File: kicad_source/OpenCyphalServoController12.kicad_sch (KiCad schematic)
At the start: 46 parts, among them CN1 RASPBERRYPI_PICO, CN2 SM04B-SRSS-TB, CN3 SM04B-SRSS-TB, CN7 CONN_02X03, SW1 SPST, U3 24LC64

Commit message: started first placement
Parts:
- gave numbers to parts that had none: 21
- renumbered C6 to C1, C9 to C3, CN2 to CN1, CN7 to CN2, CN3 to CN8, CN1 to CN9, D5 to D1, D4 to D2, R11 to R1, R13 to R17, R14 to R18, R16 to R19, R15 to R22, R9 to R7, R10 to R8, R12 to R9, U3 to U1

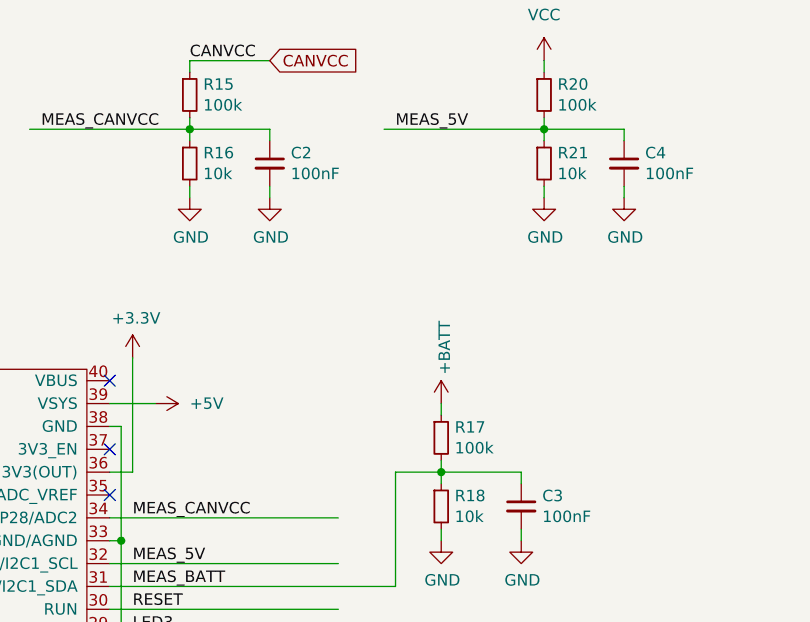
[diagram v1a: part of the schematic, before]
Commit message: corrected resistor dividers for voltage measurement
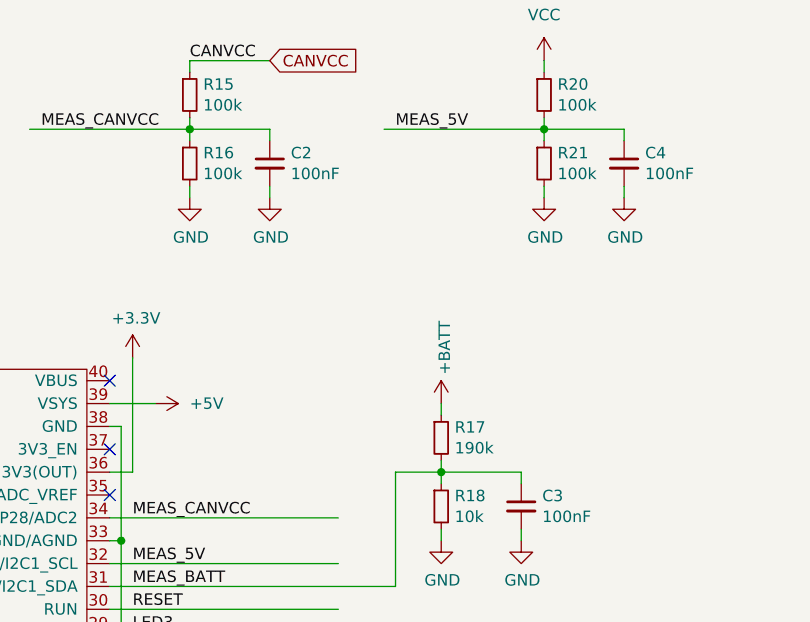
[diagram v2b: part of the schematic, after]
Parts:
- R16, R21: value 10k -> 100k
- R17: value 100k -> 190k
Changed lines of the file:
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@@
   (title_block
     (title "OpenCyphalServoController12")
-    (date "2023-01-23")
+    (date "2023-02-03")
     (rev "0.1")
     (company "generationmake")
@@
       (effects (font (size 1.27 1.27)) (justify left))
     )
-    (property "Value" "100k" (id 1) (at 245.3386 72.263 0)
+    (property "Value" "190k" (id 1) (at 245.3386 72.263 0)
       (effects (font (size 1.27 1.27)) (justify left))
     )
@@
       (effects (font (size 1.27 1.27)) (justify left))
     )
-    (property "Value" "10k" (id 1) (at 217.3986 41.783 0)
+    (property "Value" "100k" (id 1) (at 217.3986 41.783 0)
       (effects (font (size 1.27 1.27)) (justify left))
     )
@@
       (effects (font (size 1.27 1.27)) (justify left))
     )
-    (property "Value" "10k" (id 1) (at 256.7686 41.783 0)
+    (property "Value" "100k" (id 1) (at 256.7686 41.783 0)
       (effects (font (size 1.27 1.27)) (justify left))
     )
@@
     )
     (path "/98af084b-1d38-47e5-ba4f-133aa91a9cd0"
-      (reference "R16") (unit 1) (value "10k") (footprint "Resistor_SMD:R_0603_1608Metric")
+      (reference "R16") (unit 1) (value "100k") (footprint "Resistor_SMD:R_0603_1608Metric")
     )
     (path "/00000000-0000-0000-0000-000062580a99"
-      (reference "R17") (unit 1) (value "100k") (footprint "Resistor_SMD:R_0603_1608Metric")
+      (reference "R17") (unit 1) (value "190k") (footprint "Resistor_SMD:R_0603_1608Metric")
     )
     (path "/00000000-0000-0000-0000-000062580f1d"
@@
     )
     (path "/ff297292-bcb8-44b1-8fc4-6cf1ba8617ce"
-      (reference "R21") (unit 1) (value "10k") (footprint "Resistor_SMD:R_0603_1608Metric")
+      (reference "R21") (unit 1) (value "100k") (footprint "Resistor_SMD:R_0603_1608Metric")
     )
     (path "/00000000-0000-0000-0000-0000625730ad"

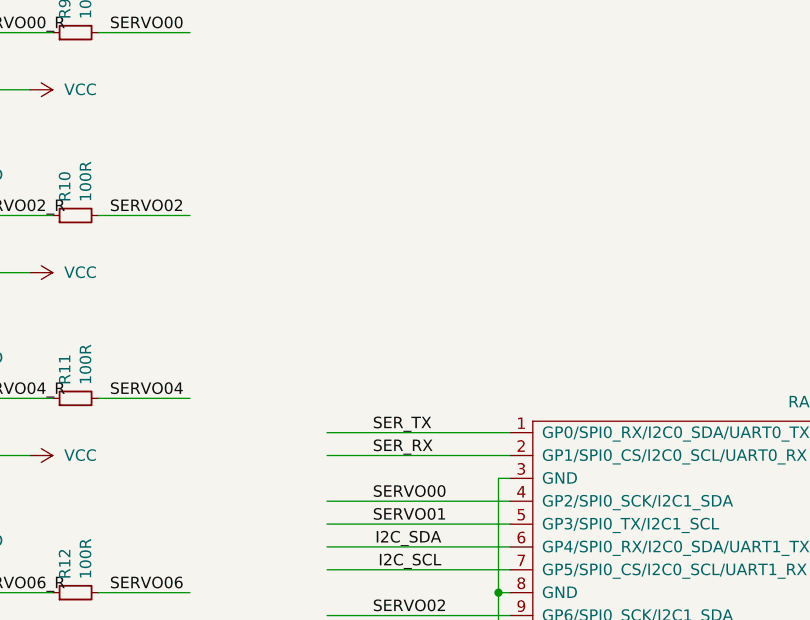
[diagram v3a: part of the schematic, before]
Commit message: added enable and power good for voltage regulator
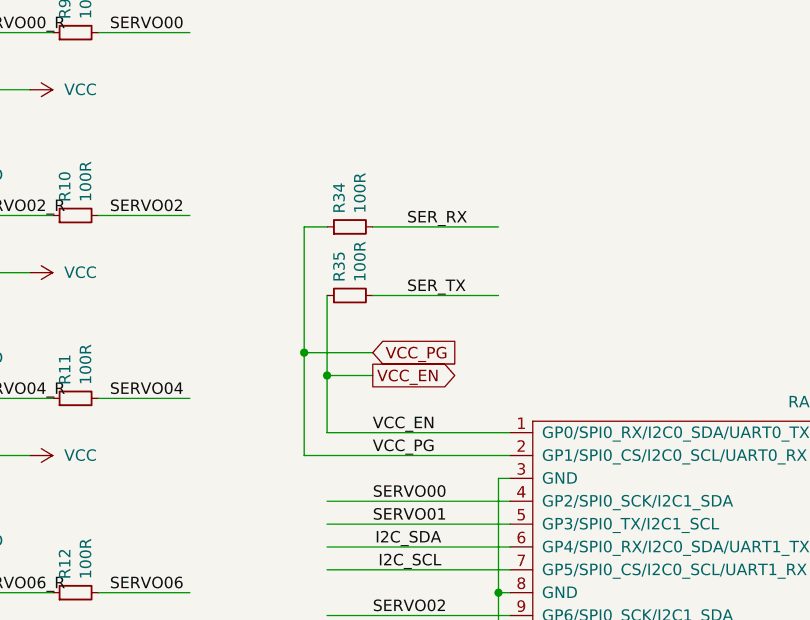
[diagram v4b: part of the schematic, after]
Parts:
- added R34, R35: 100R, Resistor_SMD:R_0603_1608Metric, symbol Device:R_Small
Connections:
- net SER_RX: now also R34.2; no longer CN9.2 (GP1/SPI0_CS/I2C0_SCL/UART0_RX)
- net SER_TX: now also R35.2; no longer CN9.1 (GP0/SPI0_RX/I2C0_SDA/UART0_TX)
- new net VCC_EN: CN9.1 (GP0/SPI0_RX/I2C0_SDA/UART0_TX), R35.1
- new net VCC_PG: CN9.2 (GP1/SPI0_CS/I2C0_SCL/UART0_RX), R34.1
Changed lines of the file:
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@@
   (junction (at 215.9 36.83) (diameter 0) (color 0 0 0 0)
   )
+  (junction (at 107.95 58.42) (diameter 0) (color 0 0 0 0)
+  )
   (junction (at 95.25 181.61) (diameter 0) (color 0 0 0 0)
   )
@@
   )
   (junction (at 208.28 82.55) (diameter 0) (color 0 0 0 0)
+  )
+  (junction (at 105.41 55.88) (diameter 0) (color 0 0 0 0)
   )
   (junction (at 95.25 179.07) (diameter 0) (color 0 0 0 0)
@@
     (stroke (width 0) (type default) (color 0 0 0 0))
   )
+  (wire (pts (xy 105.41 67.31) (xy 105.41 55.88))
+    (stroke (width 0) (type default) (color 0 0 0 0))
+  )
   (wire (pts (xy 215.9 38.1) (xy 215.9 36.83))
     (stroke (width 0) (type default) (color 0 0 0 0))
@@
     (stroke (width 0) (type default) (color 0 0 0 0))
   )
-  (wire (pts (xy 107.95 67.31) (xy 128.27 67.31))
-    (stroke (width 0) (type default) (color 0 0 0 0))
-  )
   (wire (pts (xy 95.25 176.53) (xy 95.25 179.07))
     (stroke (width 0) (type default) (color 0 0 0 0))
@@
     (stroke (width 0) (type default) (color 0 0 0 0))
   )
+  (wire (pts (xy 107.95 58.42) (xy 113.03 58.42))
+    (stroke (width 0) (type default) (color 0 0 0 0))
+  )
   (wire (pts (xy 27.94 123.19) (xy 38.1 123.19))
     (stroke (width 0) (type default) (color 0 0 0 0))
@@
     (stroke (width 0) (type default) (color 0 0 0 0))
   )
+  (wire (pts (xy 113.03 41.91) (xy 127 41.91))
+    (stroke (width 0) (type default) (color 0 0 0 0))
+  )
+  (wire (pts (xy 105.41 41.91) (xy 107.95 41.91))
+    (stroke (width 0) (type default) (color 0 0 0 0))
+  )
   (wire (pts (xy 53.34 106.68) (xy 54.61 106.68))
     (stroke (width 0) (type default) (color 0 0 0 0))
@@
     (stroke (width 0) (type default) (color 0 0 0 0))
   )
+  (wire (pts (xy 105.41 55.88) (xy 105.41 41.91))
+    (stroke (width 0) (type default) (color 0 0 0 0))
+  )
   (wire (pts (xy 228.6 105.41) (xy 207.01 105.41))
     (stroke (width 0) (type default) (color 0 0 0 0))
@@
     (stroke (width 0) (type default) (color 0 0 0 0))
   )
+  (wire (pts (xy 113.03 49.53) (xy 127 49.53))
+    (stroke (width 0) (type default) (color 0 0 0 0))
+  )
   (wire (pts (xy 237.49 36.83) (xy 255.27 36.83))
     (stroke (width 0) (type default) (color 0 0 0 0))
@@
     (stroke (width 0) (type default) (color 0 0 0 0))
   )
+  (wire (pts (xy 105.41 67.31) (xy 128.27 67.31))
+    (stroke (width 0) (type default) (color 0 0 0 0))
+  )
   (wire (pts (xy 68.58 40.64) (xy 68.58 44.45))
     (stroke (width 0) (type default) (color 0 0 0 0))
@@
     (stroke (width 0) (type default) (color 0 0 0 0))
   )
+  (wire (pts (xy 107.95 49.53) (xy 107.95 58.42))
+    (stroke (width 0) (type default) (color 0 0 0 0))
+  )
   (wire (pts (xy 120.65 177.8) (xy 120.65 181.61))
     (stroke (width 0) (type default) (color 0 0 0 0))
@@
     (stroke (width 0) (type default) (color 0 0 0 0))
   )
+  (wire (pts (xy 105.41 55.88) (xy 113.03 55.88))
+    (stroke (width 0) (type default) (color 0 0 0 0))
+  )
   (wire (pts (xy 54.61 111.76) (xy 52.07 111.76))
     (stroke (width 0) (type default) (color 0 0 0 0))
@@
   )
   (wire (pts (xy 69.85 91.44) (xy 69.85 93.98))
+    (stroke (width 0) (type default) (color 0 0 0 0))
+  )
+  (wire (pts (xy 107.95 58.42) (xy 107.95 64.77))
     (stroke (width 0) (type default) (color 0 0 0 0))
   )
@@
     (effects (font (size 1.27 1.27)) (justify right bottom))
   )
-  (label "SER_TX" (at 113.03 64.77 0)
+  (label "VCC_EN" (at 113.03 64.77 0)
     (effects (font (size 1.27 1.27)) (justify left bottom))
   )
@@
     (effects (font (size 1.27 1.27)) (justify left bottom))
   )
-  (label "SER_RX" (at 113.03 67.31 0)
+  (label "VCC_PG" (at 113.03 67.31 0)
     (effects (font (size 1.27 1.27)) (justify left bottom))
   )
@@
     (effects (font (size 1.27 1.27)) (justify left bottom))
   )
+  (label "SER_TX" (at 116.84 49.53 0)
+    (effects (font (size 1.27 1.27)) (justify left bottom))
+  )
   (label "SERVO00" (at 113.03 72.39 0)
     (effects (font (size 1.27 1.27)) (justify left bottom))
@@
     (effects (font (size 1.27 1.27)) (justify right bottom))
   )
+  (label "SER_RX" (at 116.84 41.91 0)
+    (effects (font (size 1.27 1.27)) (justify left bottom))
+  )
   (label "MCP2515_CS" (at 209.55 110.49 0)
     (effects (font (size 1.27 1.27)) (justify left bottom))
+  )
+  (global_label "VCC_PG" (shape input) (at 113.03 55.88 0) (fields_autoplaced)
+    (effects (font (size 1.27 1.27)) (justify left))
+    (property "Referenzen zwischen Schaltplänen" "${INTERSHEET_REFS}" (id 0) (at 122.4904 55.8006 0)
+      (effects (font (size 1.27 1.27)) (justify left) hide)
+    )
   )
   (global_label "MISO" (shape input) (at 228.6 113.03 0) (fields_autoplaced)
@@
     (property "Referenzen zwischen Schaltplänen" "${INTERSHEET_REFS}" (id 0) (at -5.08 25.4 0)
       (effects (font (size 1.27 1.27)) hide)
+    )
+  )
+  (global_label "VCC_EN" (shape output) (at 113.03 58.42 0) (fields_autoplaced)
+    (effects (font (size 1.27 1.27)) (justify left))
+    (property "Referenzen zwischen Schaltplänen" "${INTERSHEET_REFS}" (id 0) (at 122.4299 58.3406 0)
+      (effects (font (size 1.27 1.27)) (justify left) hide)
     )
   )
@@
     (pin "1")
   )
+  (symbol (lib_id "Device:R_Small") (at 110.49 41.91 90) (unit 1)
+    (in_bom yes) (on_board yes)
+    (property "Reference" "R34" (id 0) (at 109.3216 40.4114 0)
+      (effects (font (size 1.27 1.27)) (justify left))
+    )
+    (property "Value" "100R" (id 1) (at 111.633 40.4114 0)
+      (effects (font (size 1.27 1.27)) (justify left))
+    )
+    (property "Footprint" "Resistor_SMD:R_0603_1608Metric" (id 2) (at 114.3 41.91 0)
+      (effects (font (size 1.27 1.27)) hide)
+    )
+    (property "Datasheet" "" (id 3) (at 110.49 41.91 0))
+    (pin "1")
+    (pin "2")
+  )
   (symbol (lib_id "power:VCC") (at 45.72 26.67 90) (unit 1)
     (in_bom yes) (on_board yes) (fields_autoplaced)
@@
     (property "Datasheet" "" (id 3) (at 69.85 93.98 0))
     (pin "1")
+  )
+  (symbol (lib_id "Device:R_Small") (at 110.49 49.53 90) (unit 1)
+    (in_bom yes) (on_board yes)
+    (property "Reference" "R35" (id 0) (at 109.3216 48.0314 0)
+      (effects (font (size 1.27 1.27)) (justify left))
+    )
+    (property "Value" "100R" (id 1) (at 111.633 48.0314 0)
+      (effects (font (size 1.27 1.27)) (justify left))
+    )
+    (property "Footprint" "Resistor_SMD:R_0603_1608Metric" (id 2) (at 114.3 49.53 0)
+      (effects (font (size 1.27 1.27)) hide)
+    )
+    (property "Datasheet" "" (id 3) (at 110.49 49.53 0))
+    (pin "1")
+    (pin "2")
   )
   (symbol (lib_id "OpenCyphalPicoBase-rescue:CONN_02X03-mechanical-connectors") (at 60.96 46.99 0) (unit 1)
@@
       (reference "R33") (unit 1) (value "2k2") (footprint "Resistor_SMD:R_0603_1608Metric")
     )
+    (path "/1bcb32a0-a5af-4de2-90ae-bca31114dd14"
+      (reference "R34") (unit 1) (value "100R") (footprint "Resistor_SMD:R_0603_1608Metric")
+    )
+    (path "/8c41bdaa-0a38-47f7-9427-66d23583f756"
+      (reference "R35") (unit 1) (value "100R") (footprint "Resistor_SMD:R_0603_1608Metric")
+    )
     (path "/00000000-0000-0000-0000-000062c04ae1"

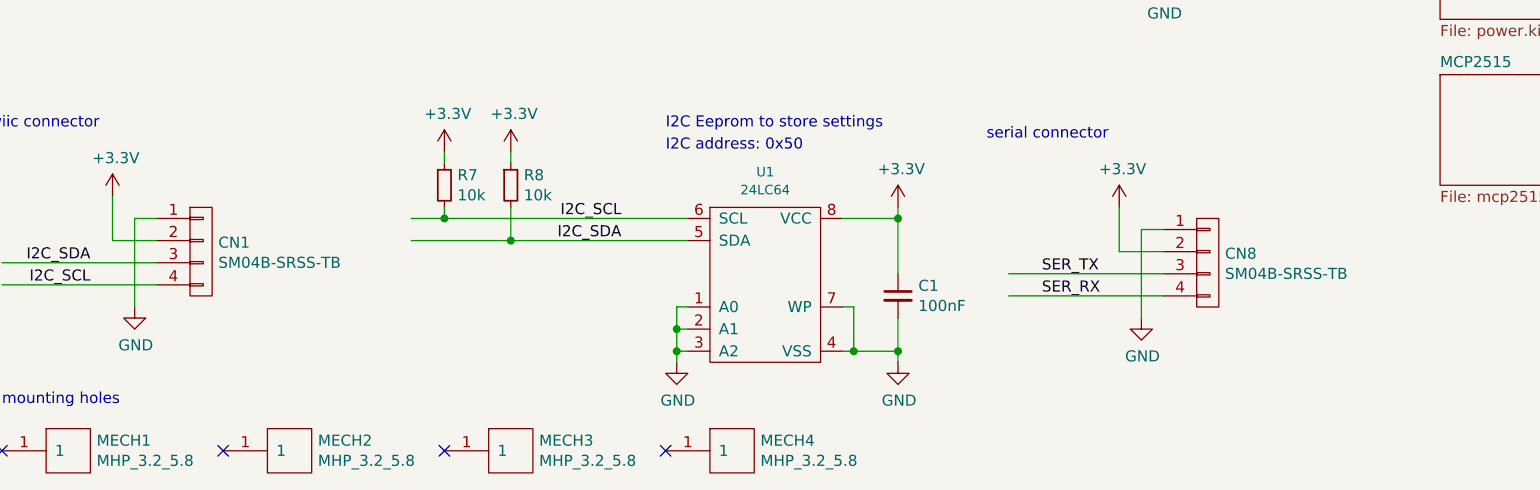
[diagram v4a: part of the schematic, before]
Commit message: added mounting pads, beautified layout, run DRC
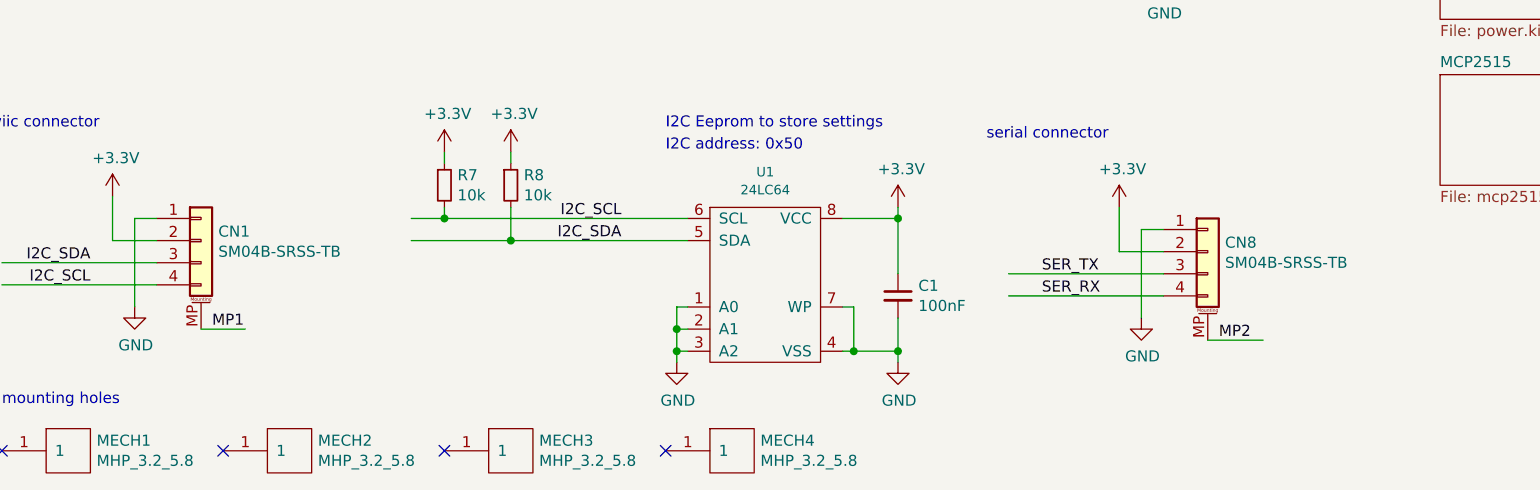
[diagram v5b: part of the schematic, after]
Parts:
- CN1, CN8: symbol OpenCyphalPicoBase-rescue:CONN_01X04-mechanical-connectors -> Connector_Generic_MountingPin:Conn_01x04_MountingPin
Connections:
- new net MP1: CN1.MP (MountPin)
- new net MP2: CN8.MP (MountPin)
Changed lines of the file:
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@@
   (title_block
     (title "OpenCyphalServoController12")
-    (date "2023-02-03")
+    (date "2023-02-04")
     (rev "0.1")
     (company "generationmake")
@@
     (stroke (width 0) (type default) (color 0 0 0 0))
   )
+  (wire (pts (xy 40.64 179.07) (xy 45.72 179.07))
+    (stroke (width 0) (type default) (color 0 0 0 0))
+  )
   (wire (pts (xy 207.01 69.85) (xy 208.28 69.85))
     (stroke (width 0) (type default) (color 0 0 0 0))
@@
     (stroke (width 0) (type default) (color 0 0 0 0))
   )
+  (wire (pts (xy 156.21 180.34) (xy 162.56 180.34))
+    (stroke (width 0) (type default) (color 0 0 0 0))
+  )
   (wire (pts (xy 67.31 91.44) (xy 69.85 91.44))
     (stroke (width 0) (type default) (color 0 0 0 0))
@@
     (effects (font (size 1.27 1.27)) (justify left bottom))
   )
+  (label "MP1" (at 41.91 179.07 0)
+    (effects (font (size 1.27 1.27)) (justify left bottom))
+  )
   (label "SERVO01" (at 36.83 20.32 180)
     (effects (font (size 1.27 1.27)) (justify right bottom))
@@
   )
   (label "SERVO00_R" (at 68.58 20.32 0)
+    (effects (font (size 1.27 1.27)) (justify left bottom))
+  )
+  (label "MP2" (at 157.48 180.34 0)
     (effects (font (size 1.27 1.27)) (justify left bottom))
   )
@@
     (pin "1")
   )
-  (symbol (lib_id "OpenCyphalPicoBase-rescue:CONN_01X04-mechanical-connectors") (at 156.21 171.45 0) (unit 1)
-    (in_bom yes) (on_board yes)
-    (property "Reference" "CN8" (id 0) (at 158.1912 170.4086 0)
-      (effects (font (size 1.27 1.27)) (justify left))
-    )
-    (property "Value" "SM04B-SRSS-TB" (id 1) (at 158.1912 172.72 0)
-      (effects (font (size 1.27 1.27)) (justify left))
-    )
-    (property "Footprint" "Connector_JST:JST_SH_SM04B-SRSS-TB_1x04-1MP_P1.00mm_Horizontal" (id 2) (at 156.21 171.45 0)
-      (effects (font (size 1.27 1.27)) hide)
-    )
-    (property "Datasheet" "" (id 3) (at 156.21 171.45 0))
+  (symbol (lib_id "Connector_Generic_MountingPin:Conn_01x04_MountingPin") (at 156.21 170.18 0) (unit 1)
+    (in_bom yes) (on_board yes)
+    (property "Reference" "CN8" (id 0) (at 158.1912 169.1386 0)
+      (effects (font (size 1.27 1.27)) (justify left))
+    )
+    (property "Value" "SM04B-SRSS-TB" (id 1) (at 158.1912 171.45 0)
+      (effects (font (size 1.27 1.27)) (justify left))
+    )
+    (property "Footprint" "Connector_JST:JST_SH_SM04B-SRSS-TB_1x04-1MP_P1.00mm_Horizontal" (id 2) (at 156.21 170.18 0)
+      (effects (font (size 1.27 1.27)) hide)
+    )
+    (property "Datasheet" "~" (id 3) (at 156.21 170.18 0)
+      (effects (font (size 1.27 1.27)) hide)
+    )
     (pin "1")
     (pin "2")
     (pin "3")
     (pin "4")
+    (pin "MP")
   )
   (symbol (lib_id "OpenCyphalPicoBase-rescue:GND-power-supply") (at 148.59 177.8 0) (unit 1)
@@
     (pin "1")
   )
-  (symbol (lib_id "OpenCyphalPicoBase-rescue:CONN_01X04-mechanical-connectors") (at 40.64 170.18 0) (unit 1)
-    (in_bom yes) (on_board yes)
-    (property "Reference" "CN1" (id 0) (at 42.6212 169.1386 0)
-      (effects (font (size 1.27 1.27)) (justify left))
-    )
-    (property "Value" "SM04B-SRSS-TB" (id 1) (at 42.6212 171.45 0)
-      (effects (font (size 1.27 1.27)) (justify left))
-    )
-    (property "Footprint" "Connector_JST:JST_SH_SM04B-SRSS-TB_1x04-1MP_P1.00mm_Horizontal" (id 2) (at 40.64 170.18 0)
-      (effects (font (size 1.27 1.27)) hide)
-    )
-    (property "Datasheet" "" (id 3) (at 40.64 170.18 0))
+  (symbol (lib_id "Connector_Generic_MountingPin:Conn_01x04_MountingPin") (at 40.64 168.91 0) (unit 1)
+    (in_bom yes) (on_board yes)
+    (property "Reference" "CN1" (id 0) (at 42.6212 167.8686 0)
+      (effects (font (size 1.27 1.27)) (justify left))
+    )
+    (property "Value" "SM04B-SRSS-TB" (id 1) (at 42.6212 170.18 0)
+      (effects (font (size 1.27 1.27)) (justify left))
+    )
+    (property "Footprint" "Connector_JST:JST_SH_SM04B-SRSS-TB_1x04-1MP_P1.00mm_Horizontal" (id 2) (at 40.64 168.91 0)
+      (effects (font (size 1.27 1.27)) hide)
+    )
+    (property "Datasheet" "~" (id 3) (at 40.64 168.91 0)
+      (effects (font (size 1.27 1.27)) hide)
+    )
     (pin "1")
     (pin "2")
     (pin "3")
     (pin "4")
+    (pin "MP")
   )
   (symbol (lib_id "OpenCyphalPicoBase-rescue:+3.3V-power-supply") (at 30.48 163.83 0) (unit 1)
